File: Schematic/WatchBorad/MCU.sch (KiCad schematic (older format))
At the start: 57 parts, among them J1 Conn_01x07_Female, U1 BNO055, U11 GC9A01, U2 nRF52832-QFxx, U3 CAT4002ATD-GT3, U4 MX25R1635F, X1 Crystal_GND24_Small, X2 Crystal_Small

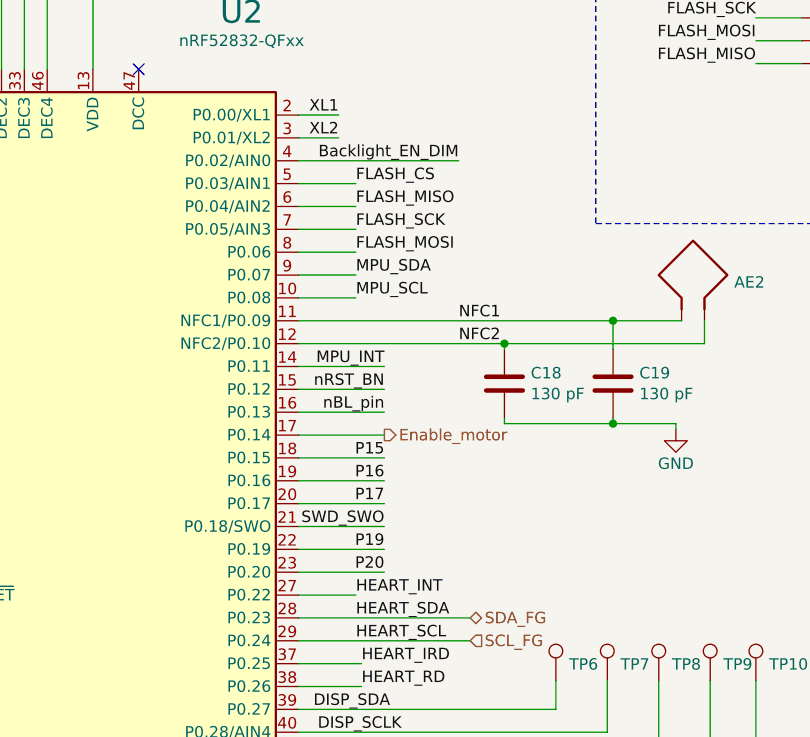
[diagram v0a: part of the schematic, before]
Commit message: Added more routings for components.Moved MCU to the top layer. Added 4-layer board setup
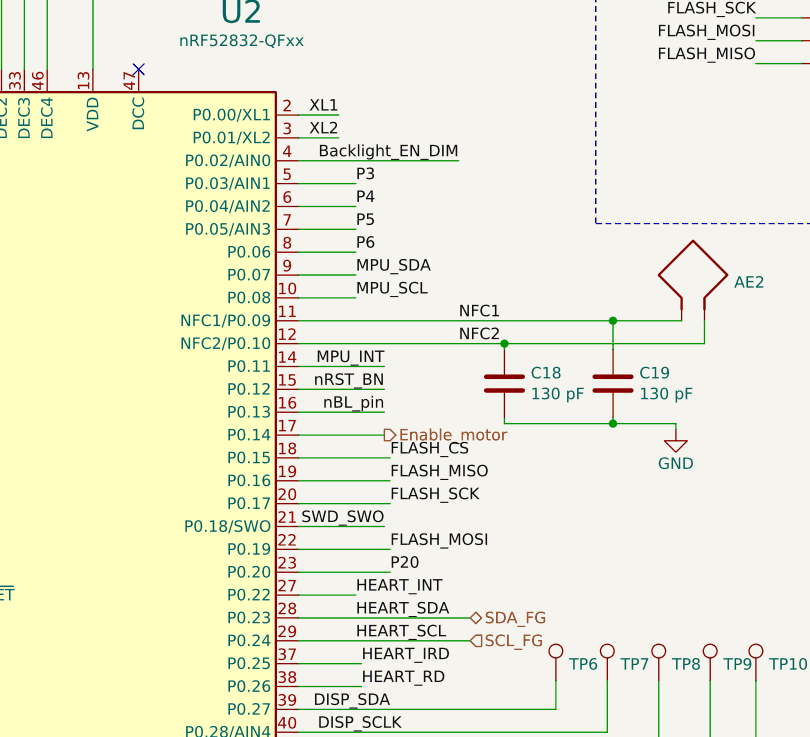
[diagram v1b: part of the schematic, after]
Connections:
- net labels added: P3, P4, P5, P6
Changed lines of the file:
@@
 Text Notes 8925 725  0    50   ~ 0
 SPI FLASH Memory\n
-Text Label 6600 2150 0    50   ~ 0
-FLASH_CS
-Text Label 6600 2250 0    50   ~ 0
-FLASH_MISO
-Text Label 6600 2350 0    50   ~ 0
+Text Label 6750 3550 0    50   ~ 0
 FLASH_SCK
-Text Label 6600 2450 0    50   ~ 0
+Text Label 6750 3750 0    50   ~ 0
 FLASH_MOSI
 Wire Wire Line
@@
 Wire Wire Line
 	6350 2450 6600 2450
-Wire Wire Line
-	6725 3450 6350 3450
-Wire Wire Line
-	6725 3550 6350 3550
-Text Label 6725 3450 2    50   ~ 0
-P16
-Text Label 6725 3550 2    50   ~ 0
-P17
-Wire Wire Line
-	6725 3750 6350 3750
-Wire Wire Line
-	6725 3850 6350 3850
-Text Label 6725 3750 2    50   ~ 0
-P19
-Text Label 6725 3850 2    50   ~ 0
-P20
-Text Label 6725 3350 2    50   ~ 0
-P15
-Wire Wire Line
-	6725 3350 6350 3350
 Text HLabel 1100 2475 2    50   Input ~ 0
 PB_1_MCU
@@
 	1    0    0    -1
 $EndComp
+Text Label 6750 3350 0    50   ~ 0
+FLASH_CS
+Text Label 6750 3450 0    50   ~ 0
+FLASH_MISO
+Wire Wire Line
+	6350 3350 6750 3350
+Wire Wire Line
+	6350 3450 6750 3450
+Wire Wire Line
+	6350 3550 6750 3550
+Wire Wire Line
+	6350 3750 6750 3750
+Text Label 6600 2150 0    50   ~ 0
+P3
+Text Label 6600 2250 0    50   ~ 0
+P4
+Text Label 6600 2350 0    50   ~ 0
+P5
+Text Label 6600 2450 0    50   ~ 0
+P6
+Text Label 6750 3850 0    50   ~ 0
+P20
+Wire Wire Line
+	6350 3850 6750 3850
 $EndSCHEMATC

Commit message: Fixed Type-C position. Added 3Dmodel for winbond
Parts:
- U4: lcsc https://lcsc.com/product-detail/FLASH_MXIC-Macronix-MX25R16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 -> https://lcsc.com/product-detail/FLASH_Winbond-Elec-W25Q128J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
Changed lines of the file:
@@
 F 1 "MX25R1635F" H 9250 2104 50  0000 C CNN
 F 2 "LocalFootprints:W25Q128JVPIQ" H 9250 1525 50  0001 L BNN
-F 3 "https://datasheet.lcsc.com/szlcsc/Macronix-MX25R1635FM2IL0_C152602.pdf" H 9250 1525 50  0001 L BNN
-F 4 "https://lcsc.com/product-detail/FLASH_MXIC-Macronix-MX25R1635FM2IL0_C152602.html" H 9250 1525 50  0001 C CNN "lcsc"
+F 3 "https://datasheet.lcsc.com/lcsc/1809140423_Winbond-Elec-W25Q128JVPIQ_C190862.pdf" H 9250 1525 50  0001 L BNN
+F 4 "https://lcsc.com/product-detail/FLASH_Winbond-Elec-W25Q128JVPIQTR_C190862.html" H 9250 1525 50  0001 C CNN "lcsc"
 	1    9250 1525
 	1    0    0    -1

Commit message: Updated & fixed missed SCH parts list
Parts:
- removed C17: 100 nF, Capacitor_SMD:C_0603_1608Metric, symbol Device:C
- removed TP5: TestPoint, Measurement_Points:Measurement_Point_Round-SMD-Pad_Small, symbol Connector:TestPoint
- removed U1: BNO055, Housings_LGA:LGA-28_5.2x3.8mm_Pitch0.5mm, symbol WatchBorad-rescue:BNO055-Sensor_Motion
- added U1: LSM6DSLTR, QFN_6DSLTR_STM, symbol WatchBorad-rescue:LSM6DSLTR-2021-06-21_20-09-55
- X1: symbol WatchBorad-rescue:Crystal_GND24_Small-Device -> WatchBorad-rescue:Crystal_GND24_Small-Device-WatchBorad-rescue
- X2: footprint Crystals:Crystal_SMD_2012-2pin_2.0x1.2mm -> Crystals:Crystal_SMD_3215-2pin_3.2x1.5mm; lcsc https://lcsc.com/product-detail/SMD-Crystal-Resonators_Seik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 -> https://lcsc.com/product-detail/Crystals_TKD-SF32WK32768D31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
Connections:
- net labels added: FG_OD_ALRT_N, MPU_INT_1, MPU_INT_2, NC_PU
- net labels removed: MPU_ADO, MPU_BL_IND, MPU_INT, nBL_pin, nRST_BN
- wire segments 257 -> 245
- no-connect marks 5 -> 2
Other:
- note added: "LSM6DSL addr is 1101011b"
- note removed: "Bootloader mode\nselect pin (active low)"
- note removed: "By default, the\ninternal clock is selected"
- note removed: "Gyroscope & Accelerometer & Magnetometer with I2C interface"
- note removed: "I2C configuration COM3_state I2C address\nSlave HIGH 0x29\nSlave LOW 0x28\nHID-I2C X 0x40\n"
- note removed: "PS1 PS0 Functionality\n0 0 Standard/Fast I2C Interface\n0 1 HID over I2C\n1 0 UART Interface\n1 1 Reserved"
- note removed: "int PU"
- moved on the sheet: C14, C16, R4, R5, R6, R7, R8

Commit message: Fixed buttons layout. Added layout draft for the display testpoints [SCHEMATIC]
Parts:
- U1: symbol WatchBorad-rescue:LSM6DSLTR-2021-06-21_20-09-55 -> WatchBorad-rescue:LSM6DSLTR-2021-06-21_20-09-55-WatchBorad-rescue
- X1: symbol WatchBorad-rescue:Crystal_GND24_Small-Device-WatchBorad-rescue -> WatchBorad-rescue:Crystal_GND24_Small-Device-WatchBorad-rescue-WatchBorad-rescue
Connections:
- net DISP_CS: now also U2.19 (P0.16); no longer U2.42 (P0.30/AIN6)
- net DISP_DC: now also U2.18 (P0.15); no longer U2.41 (P0.29/AIN5)
- net DISP_RESET: now also U2.23 (P0.20); no longer U2.43 (P0.31/AIN7)
- net DISP_SCLK: now also U2.20 (P0.17); no longer U2.40 (P0.28/AIN4)
- net DISP_SDA: now also U2.22 (P0.19); no longer U2.39 (P0.27)
- net Enable_motor: now also U2.42 (P0.30/AIN6); no longer U2.17 (P0.14)
- net FLASH_CS: now also U2.40 (P0.28/AIN4); no longer U2.18 (P0.15)
- net FLASH_MISO: now also U2.39 (P0.27); no longer U2.19 (P0.16)
- net FLASH_MOSI: now also U2.41 (P0.29/AIN5); no longer U2.22 (P0.19)
- net FLASH_SCK: now also U2.43 (P0.31/AIN7); no longer U2.20 (P0.17)
- net PB_3_MCU: now also U2.17 (P0.14)
- net PB_5_MCU: no longer U2.23 (P0.20)
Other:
- moved on the sheet: AE2, C18, C19, TP10, TP6, TP7, TP8, TP9

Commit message: Added missed footprints
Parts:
- U1: footprint QFN_6DSLTR_STM -> LocalFootprints:LSM6DSLTR
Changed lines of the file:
@@
 F 0 "U1" H 3850 6737 60  0000 C CNN
 F 1 "LSM6DSLTR" H 3850 6631 60  0000 C CNN
-F 2 "QFN_6DSLTR_STM" H 3850 6590 60  0001 C CNN
+F 2 "LocalFootprints:LSM6DSLTR" H 3850 6590 60  0001 C CNN
 F 3 "" H 2950 6350 60  0000 C CNN
 	1    2950 6350

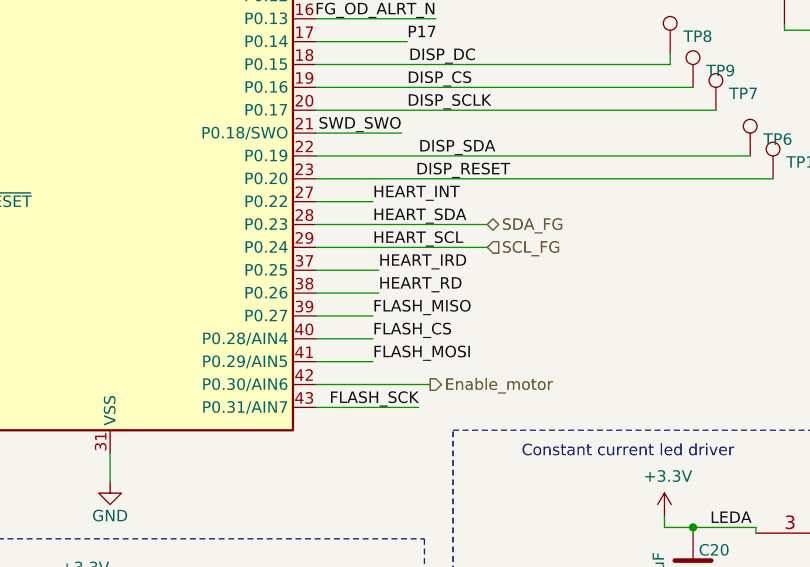
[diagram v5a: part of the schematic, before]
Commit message: Fixed buttons position
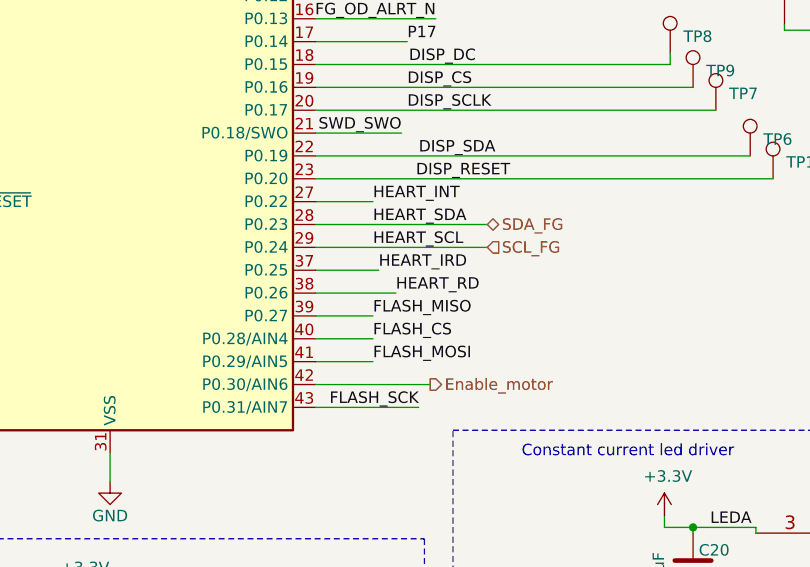
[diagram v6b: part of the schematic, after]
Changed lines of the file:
@@
 Text Label 6625 4250 0    50   ~ 0
 HEART_IRD
-Text Label 6625 4350 0    50   ~ 0
+Text Label 6700 4350 0    50   ~ 0
 HEART_RD
 Text HLabel 6850 4750 2    50   Output ~ 0
@@
 Wire Wire Line
 	6625 4250 6350 4250
-Wire Wire Line
-	6350 4350 6625 4350
 $Comp
 L Connector:TestPoint TP?
@@
 Wire Wire Line
 	6750 3250 6350 3250
+Wire Wire Line
+	6350 4350 6700 4350
 $EndSCHEMATC

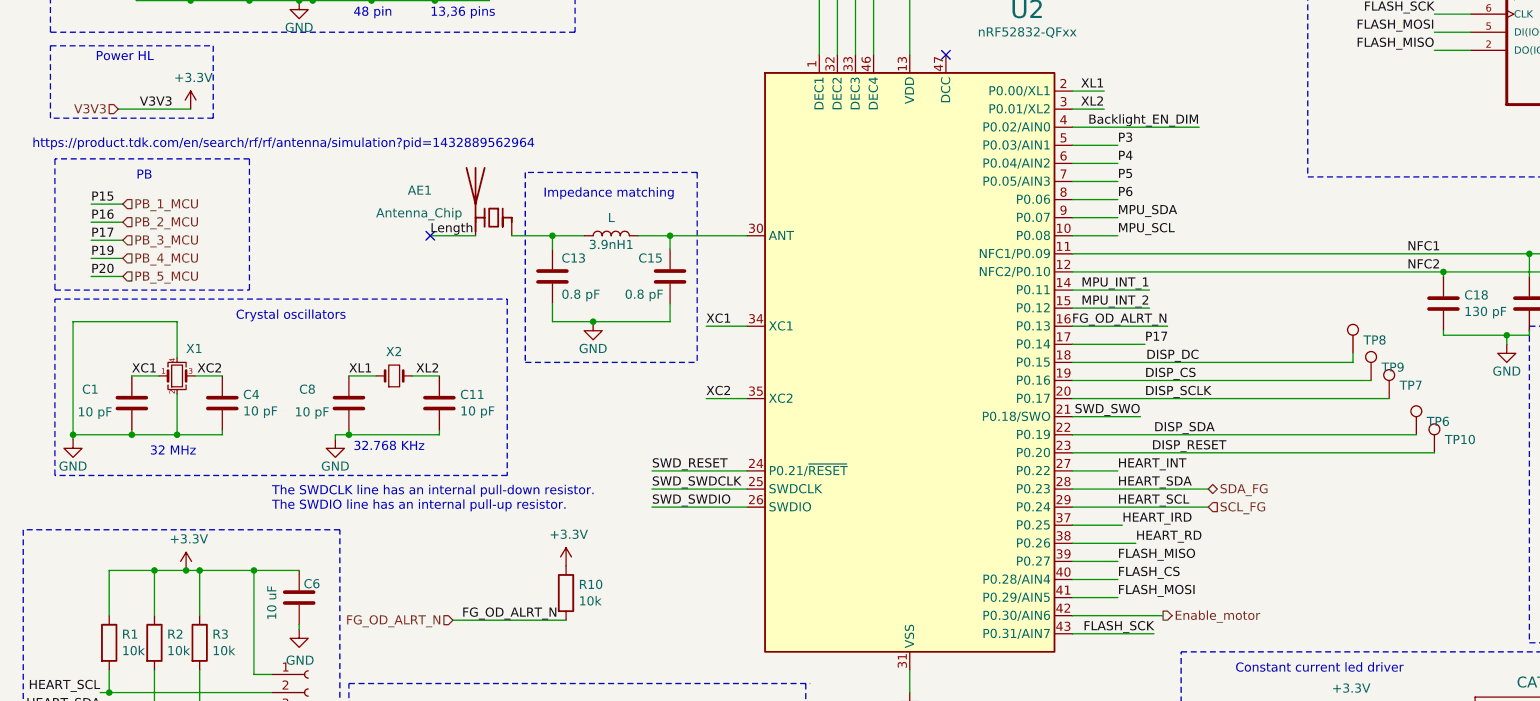
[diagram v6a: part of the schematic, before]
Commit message: Added buttons connections
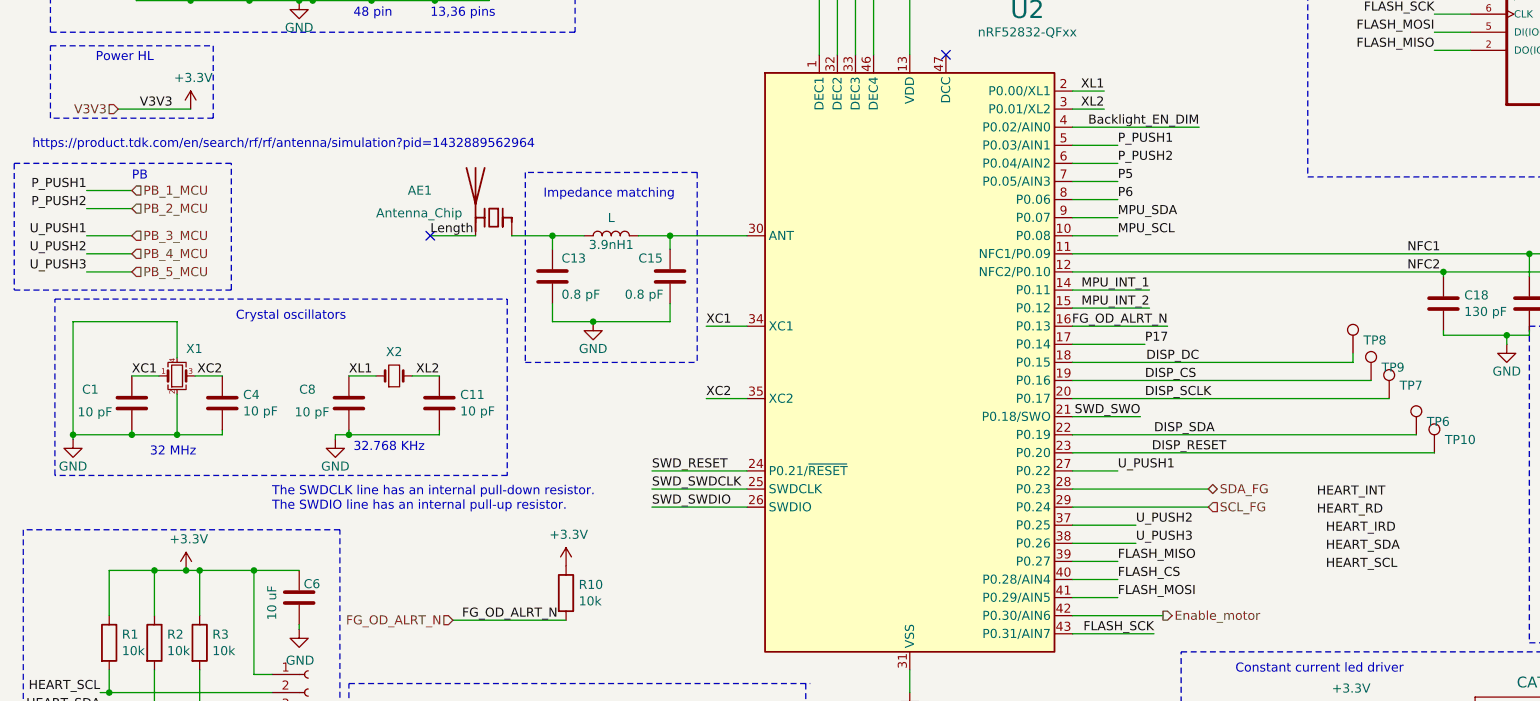
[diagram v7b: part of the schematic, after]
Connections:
- net P3 is gone; now on net PB_1_MCU: U2.5 (P0.03/AIN1)
- net P4 is gone; now on net PB_2_MCU: U2.6 (P0.04/AIN2)
- net HEART_INT: no longer U2.27 (P0.22)
- net HEART_IRD: no longer U2.37 (P0.25)
- net HEART_RD: no longer U2.38 (P0.26)
- net PB_3_MCU: now also U2.27 (P0.22); no longer U2.17 (P0.14)
- net PB_4_MCU: now also U2.37 (P0.25)
- net PB_5_MCU: now also U2.38 (P0.26)
- net SCL_FG: no longer J1.2 (Pin_2), R1.2
- net SDA_FG: no longer J1.3 (Pin_3), R2.2
- new net HEART_SCL: J1.2 (Pin_2), R1.2
- new net HEART_SDA: J1.3 (Pin_3), R2.2
- new net P17: U2.17 (P0.14)
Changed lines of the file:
@@
 Wire Wire Line
 	6350 2450 6600 2450
-Text HLabel 1100 2475 2    50   Input ~ 0
+Text HLabel 1150 2400 2    50   Input ~ 0
 PB_1_MCU
-Text HLabel 1100 2575 2    50   Input ~ 0
+Text HLabel 1150 2500 2    50   Input ~ 0
 PB_2_MCU
-Text HLabel 1100 2675 2    50   Input ~ 0
+Text HLabel 1150 2650 2    50   Input ~ 0
 PB_3_MCU
-Text HLabel 1100 2775 2    50   Input ~ 0
+Text HLabel 1150 2750 2    50   Input ~ 0
 PB_4_MCU
-Text HLabel 1100 2875 2    50   Input ~ 0
+Text HLabel 1150 2850 2    50   Input ~ 0
 PB_5_MCU
-Wire Wire Line
-	1100 2475 925  2475
-Wire Wire Line
-	1100 2575 925  2575
-Wire Wire Line
-	1100 2675 925  2675
-Wire Wire Line
-	1100 2775 925  2775
-Wire Wire Line
-	1100 2875 925  2875
-Text Label 925  2475 0    50   ~ 0
-P15
-Text Label 925  2575 0    50   ~ 0
-P16
-Text Label 925  2675 0    50   ~ 0
-P17
-Text Label 925  2775 0    50   ~ 0
-P19
-Text Label 925  2875 0    50   ~ 0
-P20
-Wire Notes Line
-	725  2950 1800 2950
-Wire Notes Line
-	1800 2950 1800 2225
-Wire Notes Line
-	1800 2225 725  2225
-Wire Notes Line
-	725  2225 725  2950
-Text Notes 1175 2350 0    50   ~ 0
+Text Notes 1150 2350 0    50   ~ 0
 PB\n
 $Comp
@@
 Wire Wire Line
 	6600 3950 6350 3950
-Text Label 6600 4050 0    50   ~ 0
+Text Label 7750 4400 0    50   ~ 0
 HEART_SDA
-Text Label 6600 3950 0    50   ~ 0
+Text Label 7700 4100 0    50   ~ 0
 HEART_INT
-Text Label 6600 4150 0    50   ~ 0
+Text Label 7750 4500 0    50   ~ 0
 HEART_SCL
 Text Label 1675 6700 0    50   ~ 0
@@
 	1    0    0    -1
 $EndComp
-Text Label 6625 4250 0    50   ~ 0
+Text Label 7750 4300 0    50   ~ 0
 HEART_IRD
-Text Label 6700 4350 0    50   ~ 0
+Text Label 7700 4200 0    50   ~ 0
 HEART_RD
 Text HLabel 6850 4750 2    50   Output ~ 0
 Enable_motor
-Wire Wire Line
-	6625 4250 6350 4250
 $Comp
 L Connector:TestPoint TP?
@@
 Text Label 6600 4450 0    50   ~ 0
 FLASH_MISO
-Text Label 6600 2150 0    50   ~ 0
-P3
-Text Label 6600 2250 0    50   ~ 0
-P4
 Text Label 6600 2350 0    50   ~ 0
 P5
@@
 Wire Wire Line
 	6350 4350 6700 4350
+Text Label 900  2750 2    50   ~ 0
+U_PUSH2
+Text Label 900  2650 2    50   ~ 0
+U_PUSH1
+Wire Wire Line
+	1150 2650 900  2650
+Wire Wire Line
+	900  2750 1150 2750
+Text Label 900  2850 2    50   ~ 0
+U_PUSH3
+Wire Wire Line
+	900  2850 1150 2850
+Text Label 900  2400 2    50   ~ 0
+P_PUSH1
+Text Label 900  2500 2    50   ~ 0
+P_PUSH2
+Wire Wire Line
+	900  2500 1150 2500
+Wire Wire Line
+	1150 2400 900  2400
+Text Label 6600 3950 0    50   ~ 0
+U_PUSH1
+Text Label 6700 4250 0    50   ~ 0
+U_PUSH2
+Wire Wire Line
+	6350 4250 6700 4250
+Text Label 6700 4350 0    50   ~ 0
+U_PUSH3
+Wire Notes Line
+	500  2950 1700 2950
+Wire Notes Line
+	1700 2950 1700 2250
+Wire Notes Line
+	1700 2250 500  2250
+Wire Notes Line
+	500  2250 500  2950
+Text Label 6600 2150 0    50   ~ 0
+P_PUSH1
+Text Label 6600 2250 0    50   ~ 0
+P_PUSH2
 $EndSCHEMATC

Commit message: Fixed board's proposals. Fixed testpoints' footprint. Fixed DRC violations. Added +5V testpoint
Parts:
- TP1, TP10, TP2, TP3, TP4, TP6, TP7, TP8, TP9: footprint Measurement_Points:Measurement_Point_Round-SMD-Pad_Small -> TestPoint:TestPoint_Pad_D2.0mm
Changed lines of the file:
@@
 F 0 "TP6" H 8308 3822 50  0000 L CNN
 F 1 "TestPoint" H 8308 3777 50  0001 L CNN
-F 2 "Measurement_Points:Measurement_Point_Round-SMD-Pad_Small" H 8450 3750 50  0001 C CNN
+F 2 "TestPoint:TestPoint_Pad_D2.0mm" H 8450 3750 50  0001 C CNN
 F 3 "~" H 8450 3750 50  0001 C CNN
 	1    8250 3750
@@
 F 0 "TP7" H 8158 3622 50  0000 L CNN
 F 1 "TestPoint" H 8158 3577 50  0001 L CNN
-F 2 "Measurement_Points:Measurement_Point_Round-SMD-Pad_Small" H 8300 3550 50  0001 C CNN
+F 2 "TestPoint:TestPoint_Pad_D2.0mm" H 8300 3550 50  0001 C CNN
 F 3 "~" H 8300 3550 50  0001 C CNN
 	1    8100 3550
@@
 F 0 "TP8" H 7958 3372 50  0000 L CNN
 F 1 "TestPoint" H 7958 3327 50  0001 L CNN
-F 2 "Measurement_Points:Measurement_Point_Round-SMD-Pad_Small" H 8100 3300 50  0001 C CNN
+F 2 "TestPoint:TestPoint_Pad_D2.0mm" H 8100 3300 50  0001 C CNN
 F 3 "~" H 8100 3300 50  0001 C CNN
 	1    7900 3300
@@
 F 0 "TP9" H 8058 3522 50  0000 L CNN
 F 1 "TestPoint" H 8058 3477 50  0001 L CNN
-F 2 "Measurement_Points:Measurement_Point_Round-SMD-Pad_Small" H 8200 3450 50  0001 C CNN
+F 2 "TestPoint:TestPoint_Pad_D2.0mm" H 8200 3450 50  0001 C CNN
 F 3 "~" H 8200 3450 50  0001 C CNN
 	1    8000 3450
@@
 F 0 "TP1" H 700 6650 50  0000 L CNN
 F 1 "TestPoint" H 733 6602 50  0001 L CNN
-F 2 "Measurement_Points:Measurement_Point_Round-SMD-Pad_Small" H 875 6575 50  0001 C CNN
+F 2 "TestPoint:TestPoint_Pad_D2.0mm" H 875 6575 50  0001 C CNN
 F 3 "~" H 875 6575 50  0001 C CNN
 	1    675  6575
@@
 F 0 "TP2" H 925 6650 50  0000 L CNN
 F 1 "TestPoint" H 958 6602 50  0001 L CNN
-F 2 "Measurement_Points:Measurement_Point_Round-SMD-Pad_Small" H 1100 6575 50  0001 C CNN
+F 2 "TestPoint:TestPoint_Pad_D2.0mm" H 1100 6575 50  0001 C CNN
 F 3 "~" H 1100 6575 50  0001 C CNN
 	1    900  6575
@@
 F 0 "TP3" H 1150 6650 50  0000 L CNN
 F 1 "TestPoint" H 1183 6602 50  0001 L CNN
-F 2 "Measurement_Points:Measurement_Point_Round-SMD-Pad_Small" H 1325 6575 50  0001 C CNN
+F 2 "TestPoint:TestPoint_Pad_D2.0mm" H 1325 6575 50  0001 C CNN
 F 3 "~" H 1325 6575 50  0001 C CNN
 	1    1125 6575
@@
 F 0 "TP4" H 1375 6650 50  0000 L CNN
 F 1 "TestPoint" H 1408 6602 50  0001 L CNN
-F 2 "Measurement_Points:Measurement_Point_Round-SMD-Pad_Small" H 1550 6575 50  0001 C CNN
+F 2 "TestPoint:TestPoint_Pad_D2.0mm" H 1550 6575 50  0001 C CNN
 F 3 "~" H 1550 6575 50  0001 C CNN
 	1    1350 6575
@@
 F 0 "TP10" H 8408 3922 50  0000 L CNN
 F 1 "TestPoint" H 8408 3877 50  0001 L CNN
-F 2 "Measurement_Points:Measurement_Point_Round-SMD-Pad_Small" H 8550 3850 50  0001 C CNN
+F 2 "TestPoint:TestPoint_Pad_D2.0mm" H 8550 3850 50  0001 C CNN
 F 3 "~" H 8550 3850 50  0001 C CNN
 	1    8350 3850
